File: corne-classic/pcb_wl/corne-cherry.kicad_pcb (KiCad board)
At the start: 2 copper layers, 152.8 x 91.4 mm, 72 parts, among them J1 MJ-4PP-9, J2 OLED, J3 Conn_01x02_Female, SW1 SW_PUSH, SW10 SW_PUSH, SW11 SW_PUSH, SW12 SW_PUSH, SW13 SW_PUSH, SW14 SW_PUSH, SW15 SW_PUSH, SW16 SW_PUSH, SW17 SW_PUSH, SW18 SW_PUSH, SW19 SW_PUSH, SW2 SW_PUSH, SW20 SW_PUSH, SW21 SW_PUSH, SW22 SW_PUSH, SW23 SW_SPDT, SW24 SW_SPDT, SW3 SW_PUSH, SW4 SW_PUSH, SW5 SW_PUSH, SW6 SW_PUSH, SW7 SW_PUSH, SW8 SW_PUSH, SW9 SW_PUSH, U1 ProMicro

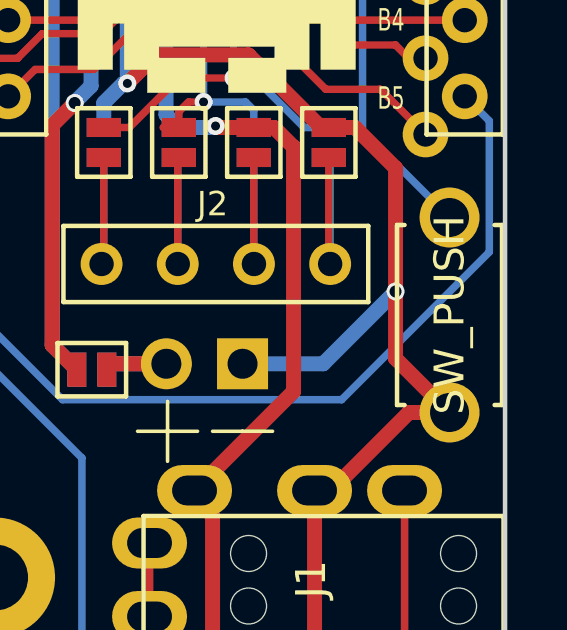
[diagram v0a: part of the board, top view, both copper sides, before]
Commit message: Fixed reset text
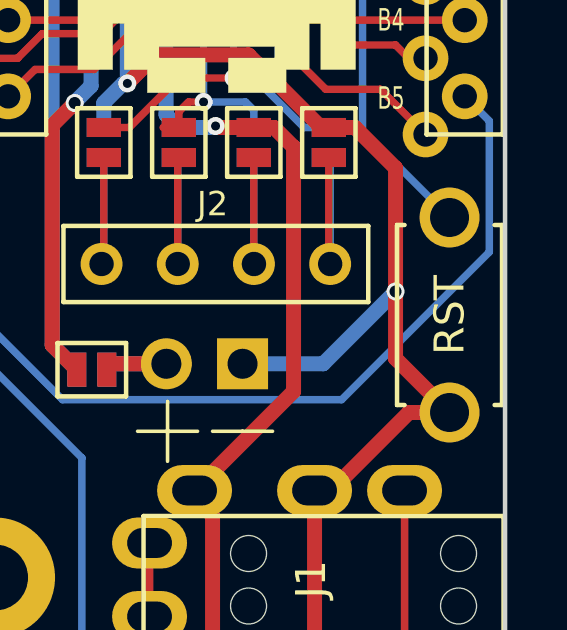
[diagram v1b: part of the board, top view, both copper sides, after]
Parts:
- RSW1: value SW_PUSH -> RST

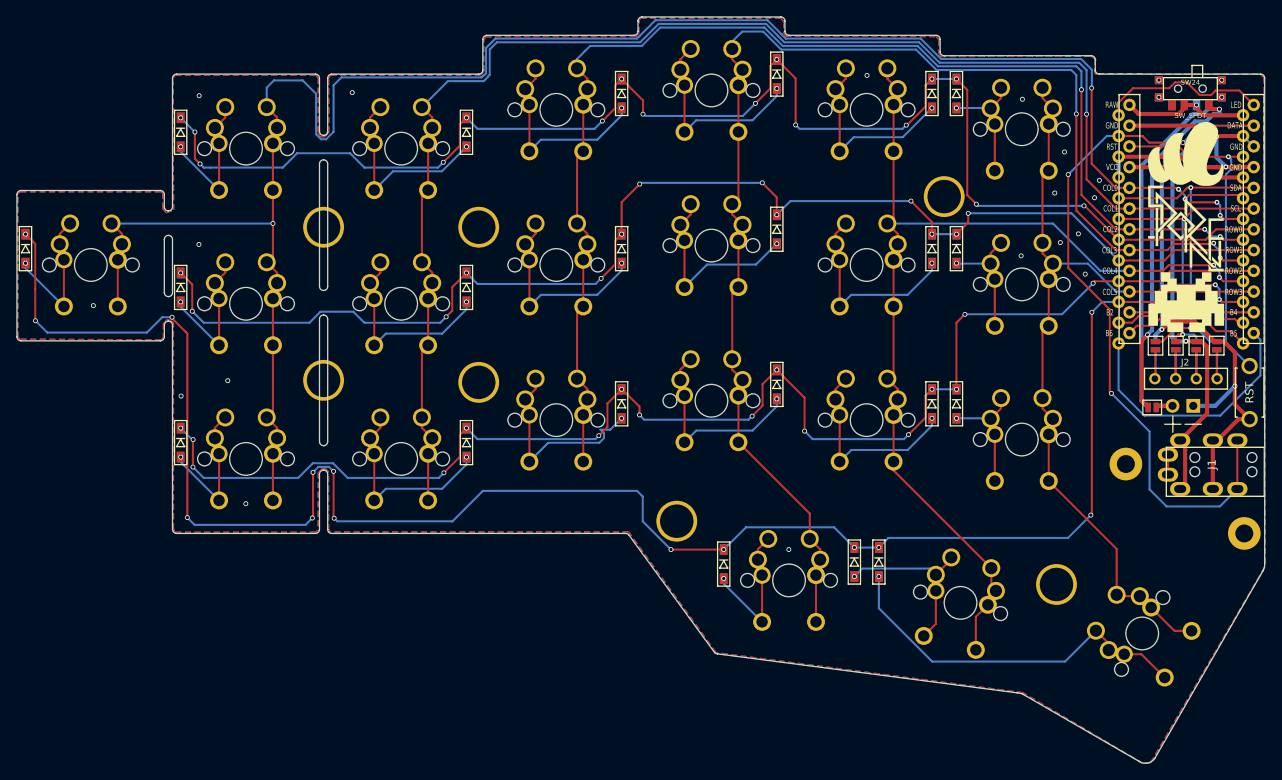
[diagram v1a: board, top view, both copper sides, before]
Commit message: Added Alps support and invertible SI thumbs
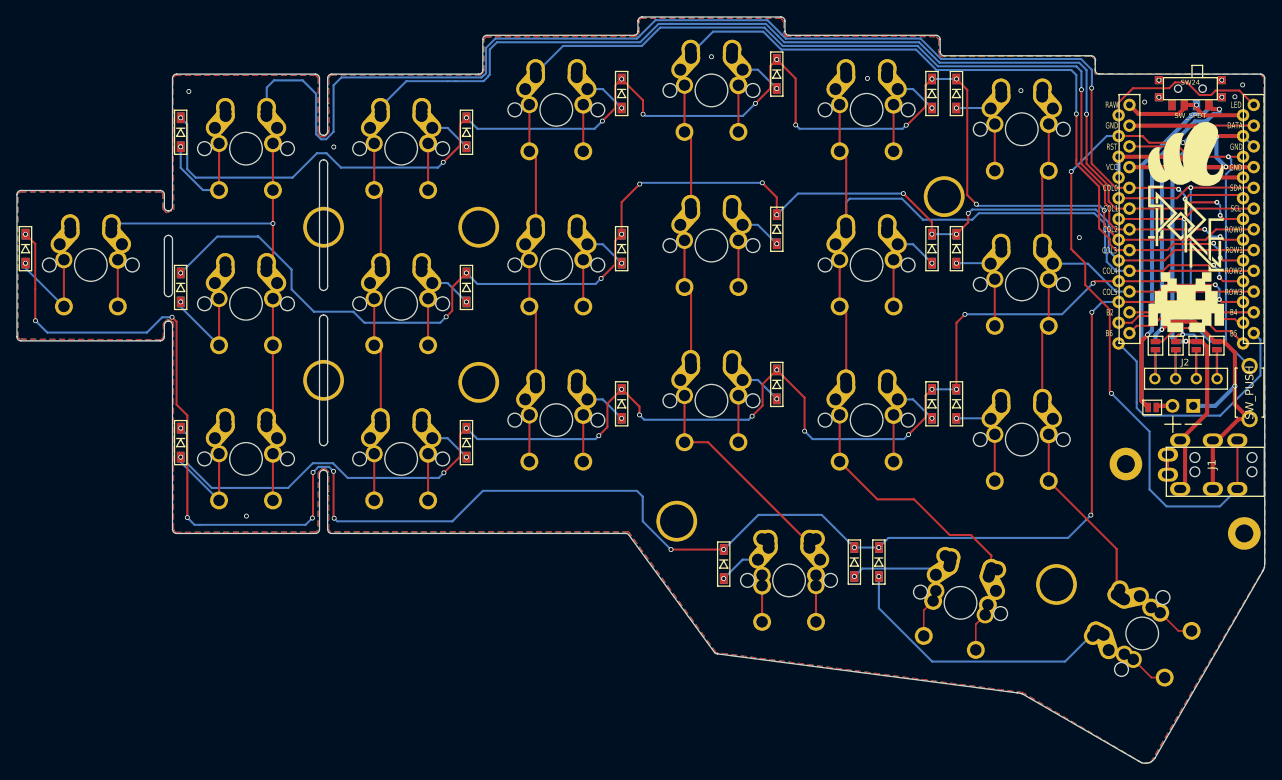
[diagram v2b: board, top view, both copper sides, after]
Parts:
- G1, G2: footprint Silks:sporne-logo-small -> sporne:sporne-logo-small
- J3: footprint kbd:Battery_Header -> sporne:Battery_Header
- RSW1: value RST -> SW_PUSH
- SW1, SW10, SW11, SW12, SW13, SW14, SW15, SW16, SW17, SW18, SW2, SW22, SW3, SW4, SW5, SW6, SW7, SW8, SW9: footprint kbd:MX_Hitek_725_1U_reversible -> sporne:MX_Alps_Hitek_725_1U_reversible
- SW19, SW20: footprint kbd:MX_Hitek_725_1U_reversible -> sporne:MX_Alps_Hitek_725_1U_reversible_thumb
- SW21: footprint kbd:MX_Hitek_725_1.5U_reversible -> sporne:MX_Alps_Hitek_725_1.5U_reversible_thumb
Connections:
- SW10 pad 1: col3 -> Net-(D10-Pad2)
- SW10 pad 2: Net-(D10-Pad2) -> col3
- SW11 pad 1: col4 -> Net-(D11-Pad2)
- SW11 pad 2: Net-(D11-Pad2) -> col4
- SW14 pad 1: col1 -> Net-(D14-Pad2)
- SW14 pad 2: Net-(D14-Pad2) -> col1
- SW15 pad 1: col2 -> Net-(D15-Pad2)
- SW15 pad 2: Net-(D15-Pad2) -> col2
- SW16 pad 1: col3 -> Net-(D16-Pad2)
- SW16 pad 2: Net-(D16-Pad2) -> col3
- SW17 pad 1: col4 -> Net-(D17-Pad2)
- SW17 pad 2: Net-(D17-Pad2) -> col4
- SW2 pad 1: col1 -> Net-(D2-Pad2)
- SW2 pad 2: Net-(D2-Pad2) -> col1
- SW3 pad 1: col2 -> Net-(D3-Pad2)
- SW3 pad 2: Net-(D3-Pad2) -> col2
- SW4 pad 1: col3 -> Net-(D4-Pad2)
- SW4 pad 2: Net-(D4-Pad2) -> col3
- SW5 pad 1: col4 -> Net-(D5-Pad2)
- SW5 pad 2: Net-(D5-Pad2) -> col4
- SW8 pad 1: col1 -> Net-(D8-Pad2)
- SW8 pad 2: Net-(D8-Pad2) -> col1
- SW9 pad 1: col2 -> Net-(D9-Pad2)
- SW9 pad 2: Net-(D9-Pad2) -> col2
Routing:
- net col4: track 127.8 -> 147.9 mm
- net Net-(D15-Pad2): track 25.6 -> 15.5 mm
- net Net-(D11-Pad2): track 24.9 -> 15.5 mm
- net Net-(D8-Pad2): track 24.9 -> 15.5 mm
- net Net-(D17-Pad2): track 24.9 -> 15.6 mm
- net Net-(D4-Pad2): track 24.9 -> 15.6 mm
- net Net-(D9-Pad2): track 24.9 -> 15.6 mm
- net Net-(D3-Pad2): track 24.9 -> 15.6 mm
- net Net-(D14-Pad2): track 24.9 -> 15.6 mm
- net Net-(D16-Pad2): track 24.9 -> 16.0 mm
- net col3: track 164.1 -> 173.1 mm
- net Net-(D5-Pad2): track 24.4 -> 15.5 mm
- net Net-(D2-Pad2): track 24.4 -> 15.5 mm
- net Net-(D10-Pad2): track 24.4 -> 15.6 mm
- net row1: track 161.6 -> 166.9 mm, vias 13 -> 12
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
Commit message: Minor fixes, updated gerbers
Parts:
- RSW1: value SW_PUSH -> RST
